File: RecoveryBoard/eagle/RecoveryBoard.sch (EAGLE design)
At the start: 96 parts, among them Q1 BSS123, Q2 BSS123, Q3 BSS123, Q4 BPR-301, Q5 BPR-301, Q6 MOSFET-PCH-SOT23-6, U1 STM32F042K6, U10 TPS63070, U2 BD62120AEFJ-E2, Y1 ECS-160-10-36Q-ES-TR

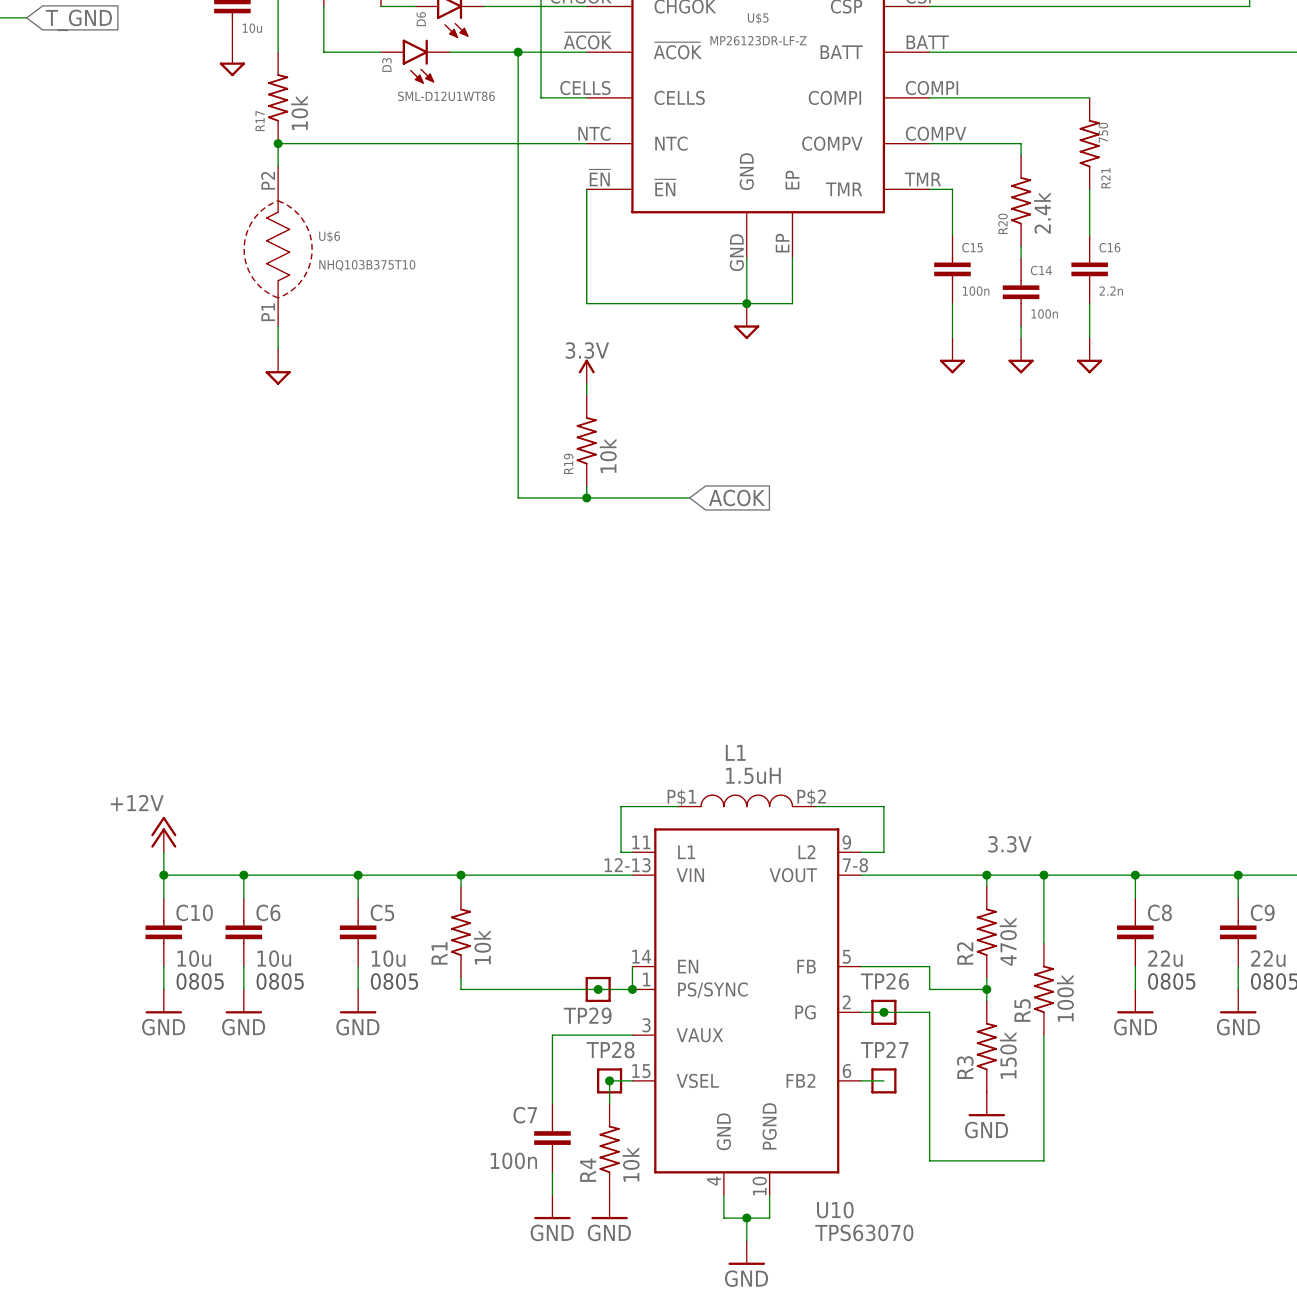
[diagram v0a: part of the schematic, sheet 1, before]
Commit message: Layout cleanup of RecoveryBoard for manufacturing. Sent off to Fab as v1.0
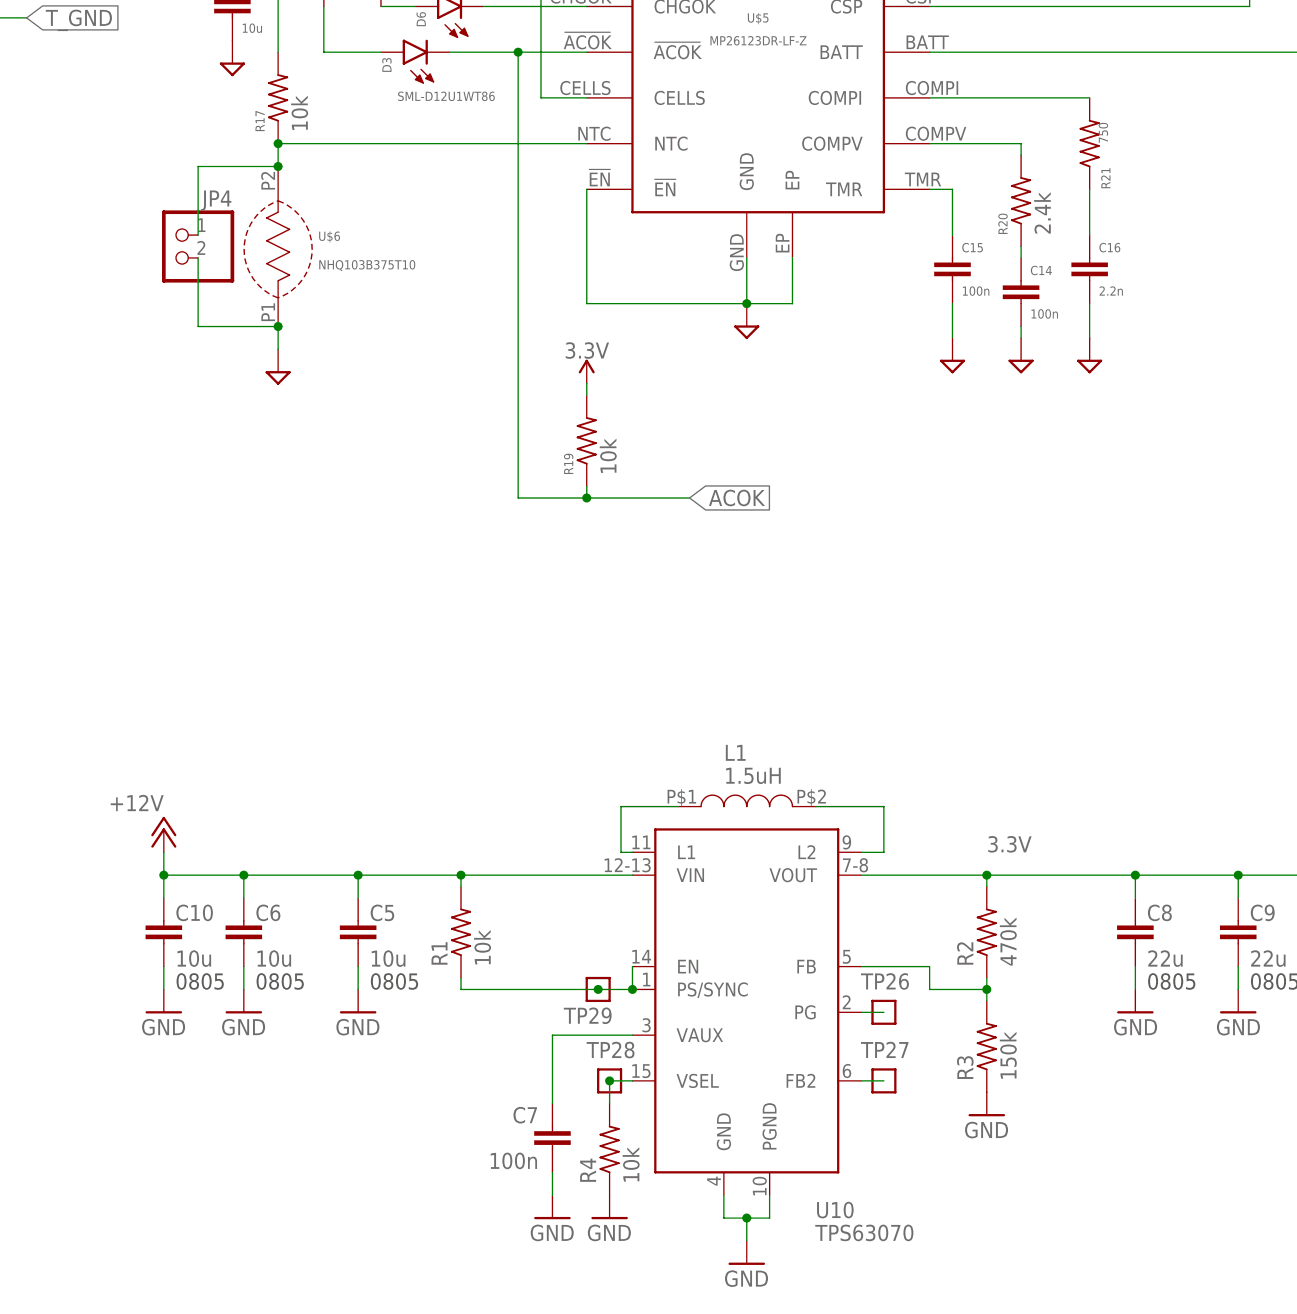
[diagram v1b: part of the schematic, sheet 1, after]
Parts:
- removed R5: 100k, oresat-rcl:R-US_0805-A-NOSILK
- added JP4: (no value), pinhead:PINHD-1X2
- C22: value 100n -> 10u
- R2: device oresat-rcl:R-US_0805-A-NOSILK -> oresat-rcl:R-US_0603-C-NOSILK
- renumbered U$3 to U3, U$4 to U5
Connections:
- removed net N$3: U2.TEST
- net 3.3V: no longer R5.2
- net GND: now also JP4.2, U2.TEST
- net N$20: now also JP4.1
- net TPS-PG: no longer R5.1
